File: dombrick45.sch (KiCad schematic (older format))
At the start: 115 parts, among them J1 AVR-ISP-6, SW1 SW_Push, U1 ATmega32U4-AU, Y1 16MHz

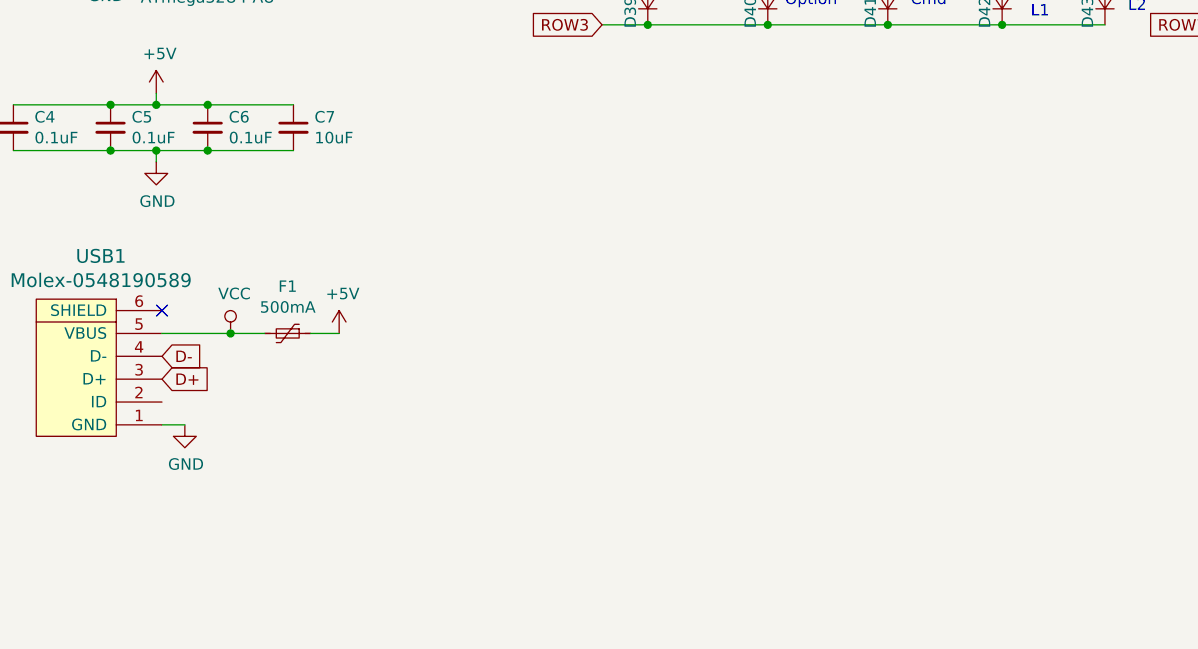
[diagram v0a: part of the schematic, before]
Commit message: 2019-10-21 usb-c impl, gnd filled and silk design completed.
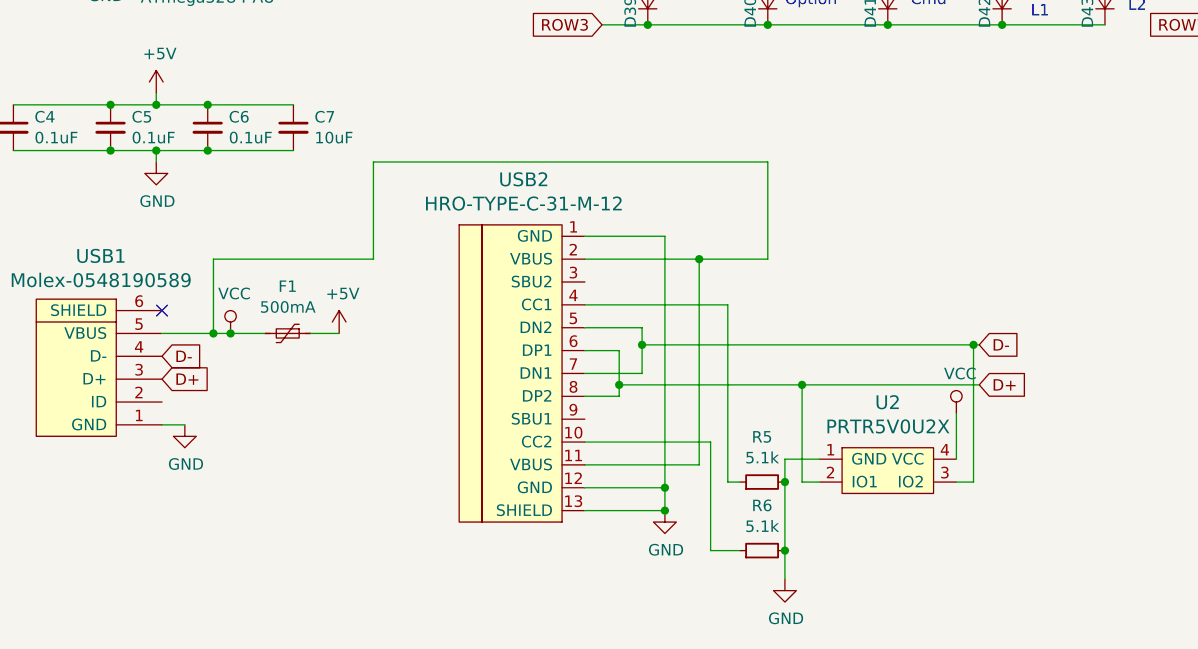
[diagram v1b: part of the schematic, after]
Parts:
- added R5, R6: 5.1k, Resistor_SMD:R_0805_2012Metric, symbol Device:R_Small
- added U2: PRTR5V0U2X, random-keyboard-parts:SOT143B, symbol random-keyboard-parts:PRTR5V0U2X
- added USB2: HRO-TYPE-C-31-M-12, Type-C:HRO-TYPE-C-31-M-12-Assembly, symbol Type-C:HRO-TYPE-C-31-M-12
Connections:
- net D+: now also U2.2 (IO1), USB2.6 (DP1), USB2.8 (DP2)
- net D-: now also U2.3 (IO2), USB2.5 (DN2), USB2.7 (DN1)
- net GND: now also R5.2, R6.2, U2.1 (GND), USB2.1 (GND), USB2.12 (GND), USB2.13 (SHIELD)
- net VCC: now also U2.4 (VCC), USB2.11 (VBUS), USB2.2 (VBUS)
- new net: R6.1, USB2.10 (CC2)
- new net: R5.1, USB2.4 (CC1)
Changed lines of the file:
@@
 COL0
 Wire Wire Line
-	2425 6300 2125 6300
+	2425 6300 2350 6300
 Connection ~ 2425 6300
 Wire Wire Line
@@
 Wire Wire Line
 	3075 1300 3675 1300
+$Comp
+L Type-C:HRO-TYPE-C-31-M-12 USB2
+U 1 1 5DB7F801
+P 3875 6425
+F 0 "USB2" H 3708 7222 60  0000 C CNN
+F 1 "HRO-TYPE-C-31-M-12" H 3708 7116 60  0000 C CNN
+F 2 "Type-C:HRO-TYPE-C-31-M-12-Assembly" H 3875 6425 60  0001 C CNN
+F 3 "" H 3875 6425 60  0001 C CNN
+	1    3875 6425
+	1    0    0    -1
+$EndComp
+Wire Wire Line
+	3975 6375 4125 6375
+Wire Wire Line
+	4125 6375 4125 6525
+Wire Wire Line
+	4125 6575 3975 6575
+Wire Wire Line
+	3975 6475 4225 6475
+Wire Wire Line
+	4225 6475 4225 6350
+Wire Wire Line
+	4225 6275 3975 6275
+Wire Wire Line
+	3975 5875 4325 5875
+Wire Wire Line
+	4325 5875 4325 6975
+Wire Wire Line
+	4325 7075 3975 7075
+Wire Wire Line
+	3975 6975 4325 6975
+Connection ~ 4325 6975
+Wire Wire Line
+	4325 6975 4325 7075
+Wire Wire Line
+	3975 5975 4475 5975
+Wire Wire Line
+	4475 5975 4475 6875
+Wire Wire Line
+	4475 6875 3975 6875
+Connection ~ 4475 5975
+$Comp
+L power:GND #PWR015
+U 1 1 5DCBEA1D
+P 4325 7075
+F 0 "#PWR015" H 4325 6825 50  0001 C CNN
+F 1 "GND" H 4330 6902 50  0000 C CNN
+F 2 "" H 4325 7075 50  0001 C CNN
+F 3 "" H 4325 7075 50  0001 C CNN
+	1    4325 7075
+	1    0    0    -1
+$EndComp
+Connection ~ 4325 7075
+Text GLabel 5700 6350 2    50   Input ~ 0
+D-
+Text GLabel 5700 6525 2    50   Input ~ 0
+D+
+Wire Wire Line
+	5700 6350 5675 6350
+Connection ~ 4225 6350
+Wire Wire Line
+	4225 6350 4225 6275
+Wire Wire Line
+	5700 6525 4925 6525
+Connection ~ 4125 6525
+Wire Wire Line
+	4125 6525 4125 6575
+$Comp
+L random-keyboard-parts:PRTR5V0U2X U2
+U 1 1 5DCF527A
+P 5300 6900
+F 0 "U2" H 5300 7197 60  0000 C CNN
+F 1 "PRTR5V0U2X" H 5300 7091 60  0000 C CNN
+F 2 "random-keyboard-parts:SOT143B" H 5300 6900 60  0001 C CNN
+F 3 "" H 5300 6900 60  0001 C CNN
+	1    5300 6900
+	1    0    0    -1
+$EndComp
+Wire Wire Line
+	5600 6850 5600 6650
+$Comp
+L Device:R_Small R5
+U 1 1 5DD3FDC7
+P 4750 6950
+F 0 "R5" V 4946 6950 50  0000 C CNN
+F 1 "5.1k" V 4855 6950 50  0000 C CNN
+F 2 "Resistor_SMD:R_0805_2012Metric" H 4750 6950 50  0001 C CNN
+F 3 "~" H 4750 6950 50  0001 C CNN
+	1    4750 6950
+	0    -1   -1   0
+$EndComp
+$Comp
+L Device:R_Small R6
+U 1 1 5DD7116B
+P 4750 7250
+F 0 "R6" V 4946 7250 50  0000 C CNN
+F 1 "5.1k" V 4855 7250 50  0000 C CNN
+F 2 "Resistor_SMD:R_0805_2012Metric" H 4750 7250 50  0001 C CNN
+F 3 "~" H 4750 7250 50  0001 C CNN
+	1    4750 7250
+	0    -1   -1   0
+$EndComp
+Wire Wire Line
+	4850 6950 4850 6850
+Wire Wire Line
+	4850 6850 5000 6850
+Wire Wire Line
+	4850 6950 4850 7250
+Connection ~ 4850 6950
+Connection ~ 4850 7250
+Wire Wire Line
+	4850 7250 4850 7375
+$Comp
+L power:GND #PWR016
+U 1 1 5DDA41FB
+P 4850 7375
+F 0 "#PWR016" H 4850 7125 50  0001 C CNN
+F 1 "GND" H 4855 7202 50  0000 C CNN
+F 2 "" H 4850 7375 50  0001 C CNN
+F 3 "" H 4850 7375 50  0001 C CNN
+	1    4850 7375
+	1    0    0    -1
+$EndComp
+Wire Wire Line
+	4650 7250 4525 7250
+Wire Wire Line
+	4525 7250 4525 6775
+Wire Wire Line
+	4525 6775 3975 6775
+Wire Wire Line
+	3975 6175 4600 6175
+Wire Wire Line
+	4600 6175 4600 6950
+Wire Wire Line
+	4600 6950 4650 6950
+Wire Wire Line
+	5000 6950 4925 6950
+Wire Wire Line
+	4925 6950 4925 6525
+Connection ~ 4925 6525
+Wire Wire Line
+	4925 6525 4125 6525
+Wire Wire Line
+	5600 6950 5675 6950
+Wire Wire Line
+	5675 6950 5675 6350
+Connection ~ 5675 6350
+Wire Wire Line
+	5675 6350 4225 6350
+$Comp
+L power:VCC #PWR014
+U 1 1 5DE0FEB4
+P 5600 6650
+F 0 "#PWR014" H 5600 6500 50  0001 C CNN
+F 1 "VCC" H 5617 6823 50  0000 C CNN
+F 2 "" H 5600 6650 50  0001 C CNN
+F 3 "" H 5600 6650 50  0001 C CNN
+	1    5600 6650
+	1    0    0    -1
+$EndComp
+Wire Wire Line
+	4475 5975 4775 5975
+Wire Wire Line
+	4775 5975 4775 5550
+Wire Wire Line
+	4775 5550 3050 5550
+Wire Wire Line
+	3050 5550 3050 5975
+Wire Wire Line
+	3050 5975 2350 5975
+Wire Wire Line
+	2350 5975 2350 6300
+Connection ~ 2350 6300
+Wire Wire Line
+	2350 6300 2125 6300
 $EndSCHEMATC

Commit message: 2019-10-22 hobo OK
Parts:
- added H1, H2, H3, H4, H5, H6, H7, H8, H9: MountingHole, MountingHole:MountingHole_2.2mm_M2, symbol Mechanical:MountingHole
- MX44: footprint MX_Only:MXOnly-2.75U-Hotswap-ReversedStabilizers -> MX_Only:MXOnly-2.75U-Hotswap
- MX49: footprint MX_Only:MXOnly-6.25U-Hotswap -> MX_Only:MXOnly-6.25U-Hotswap-ReversedStabilizers
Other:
- note added: "Dombrick means \nDvorak Oriented Mechanical\nBreakthough Remakable Interesting\nCoolest Keyboard :)"
- note removed: "Dombric means \nDvorak Oriented Mechanical\nBreakthough Remakable Interesting\nCoolest Keyboard :)"
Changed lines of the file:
@@
 COL0
 Text Notes 7025 6900 0    50   ~ 0
-Dombric means \nDvorak Oriented Mechanical\nBreakthough Remakable Interesting\nCoolest Keyboard :)
+Dombrick means \nDvorak Oriented Mechanical\nBreakthough Remakable Interesting\nCoolest Keyboard :)
 Text Notes 6850 4175 0    50   ~ 0
 X
@@
 F 0 "MX44" H 8858 4823 60  0000 C CNN
 F 1 "MX-NoLED" H 8858 4749 20  0000 C CNN
-F 2 "MX_Only:MXOnly-2.75U-Hotswap-ReversedStabilizers" H 8200 4575 60  0001 C CNN
+F 2 "MX_Only:MXOnly-2.75U-Hotswap" H 8200 4575 60  0001 C CNN
 F 3 "" H 8200 4575 60  0001 C CNN
 	1    8825 4600
@@
 F 0 "MX49" H 8858 5473 60  0000 C CNN
 F 1 "MX-NoLED" H 8858 5399 20  0000 C CNN
-F 2 "MX_Only:MXOnly-6.25U-Hotswap" H 8200 5225 60  0001 C CNN
+F 2 "MX_Only:MXOnly-6.25U-Hotswap-ReversedStabilizers" H 8200 5225 60  0001 C CNN
 F 3 "" H 8200 5225 60  0001 C CNN
 	1    8825 5250
@@
 Wire Wire Line
 	2350 6300 2125 6300
+$Comp
+L Mechanical:MountingHole H1
+U 1 1 5DCE16C5
+P 6600 5425
+F 0 "H1" H 6700 5471 50  0000 L CNN
+F 1 "MountingHole" H 6700 5380 50  0000 L CNN
+F 2 "MountingHole:MountingHole_2.2mm_M2" H 6600 5425 50  0001 C CNN
+F 3 "~" H 6600 5425 50  0001 C CNN
+	1    6600 5425
+	1    0    0    -1
+$EndComp
+$Comp
+L Mechanical:MountingHole H2
+U 1 1 5DCE1A14
+P 6825 5425
+F 0 "H2" H 6925 5471 50  0000 L CNN
+F 1 "MountingHole" H 6925 5380 50  0000 L CNN
+F 2 "MountingHole:MountingHole_2.2mm_M2" H 6825 5425 50  0001 C CNN
+F 3 "~" H 6825 5425 50  0001 C CNN
+	1    6825 5425
+	1    0    0    -1
+$EndComp
+$Comp
+L Mechanical:MountingHole H3
+U 1 1 5DCE1D28
+P 7075 5425
+F 0 "H3" H 7175 5471 50  0000 L CNN
+F 1 "MountingHole" H 7175 5380 50  0000 L CNN
+F 2 "MountingHole:MountingHole_2.2mm_M2" H 7075 5425 50  0001 C CNN
+F 3 "~" H 7075 5425 50  0001 C CNN
+	1    7075 5425
+	1    0    0    -1
+$EndComp
+$Comp
+L Mechanical:MountingHole H4
+U 1 1 5DCE1FD6
+P 7325 5425
+F 0 "H4" H 7425 5471 50  0000 L CNN
+F 1 "MountingHole" H 7425 5380 50  0000 L CNN
+F 2 "MountingHole:MountingHole_2.2mm_M2" H 7325 5425 50  0001 C CNN
+F 3 "~" H 7325 5425 50  0001 C CNN
+	1    7325 5425
+	1    0    0    -1
+$EndComp
+$Comp
+L Mechanical:MountingHole H5
+U 1 1 5DCE231D
+P 7575 5425
+F 0 "H5" H 7675 5471 50  0000 L CNN
+F 1 "MountingHole" H 7675 5380 50  0000 L CNN
+F 2 "MountingHole:MountingHole_2.2mm_M2" H 7575 5425 50  0001 C CNN
+F 3 "~" H 7575 5425 50  0001 C CNN
+	1    7575 5425
+	1    0    0    -1
+$EndComp
+$Comp
+L Mechanical:MountingHole H6
+U 1 1 5DCE2598
+P 7850 5425
+F 0 "H6" H 7950 5471 50  0000 L CNN
+F 1 "MountingHole" H 7950 5380 50  0000 L CNN
+F 2 "MountingHole:MountingHole_2.2mm_M2" H 7850 5425 50  0001 C CNN
+F 3 "~" H 7850 5425 50  0001 C CNN
+	1    7850 5425
+	1    0    0    -1
+$EndComp
+$Comp
+L Mechanical:MountingHole H7
+U 1 1 5DCE2989
+P 6675 5650
+F 0 "H7" H 6775 5696 50  0000 L CNN
+F 1 "MountingHole" H 6775 5605 50  0000 L CNN
+F 2 "MountingHole:MountingHole_2.2mm_M2" H 6675 5650 50  0001 C CNN
+F 3 "~" H 6675 5650 50  0001 C CNN
+	1    6675 5650
+	1    0    0    -1
+$EndComp
+$Comp
+L Mechanical:MountingHole H8
+U 1 1 5DCE2D36
+P 6975 5650
+F 0 "H8" H 7075 5696 50  0000 L CNN
+F 1 "MountingHole" H 7075 5605 50  0000 L CNN
+F 2 "MountingHole:MountingHole_2.2mm_M2" H 6975 5650 50  0001 C CNN
+F 3 "~" H 6975 5650 50  0001 C CNN
+	1    6975 5650
+	1    0    0    -1
+$EndComp
+$Comp
+L Mechanical:MountingHole H9
+U 1 1 5DCE3149
+P 7275 5650
+F 0 "H9" H 7375 5696 50  0000 L CNN
+F 1 "MountingHole" H 7375 5605 50  0000 L CNN
+F 2 "MountingHole:MountingHole_2.2mm_M2" H 7275 5650 50  0001 C CNN
+F 3 "~" H 7275 5650 50  0001 C CNN
+	1    7275 5650
+	1    0    0    -1
+$EndComp
 $EndSCHEMATC
